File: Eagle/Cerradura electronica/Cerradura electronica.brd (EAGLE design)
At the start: 48.5 x 50 mm, 38 parts, among them IC1 LD117AS50TR, Q1 2N3904, Q2 IRF540NS, U1 ATMEGA328P_TQFP

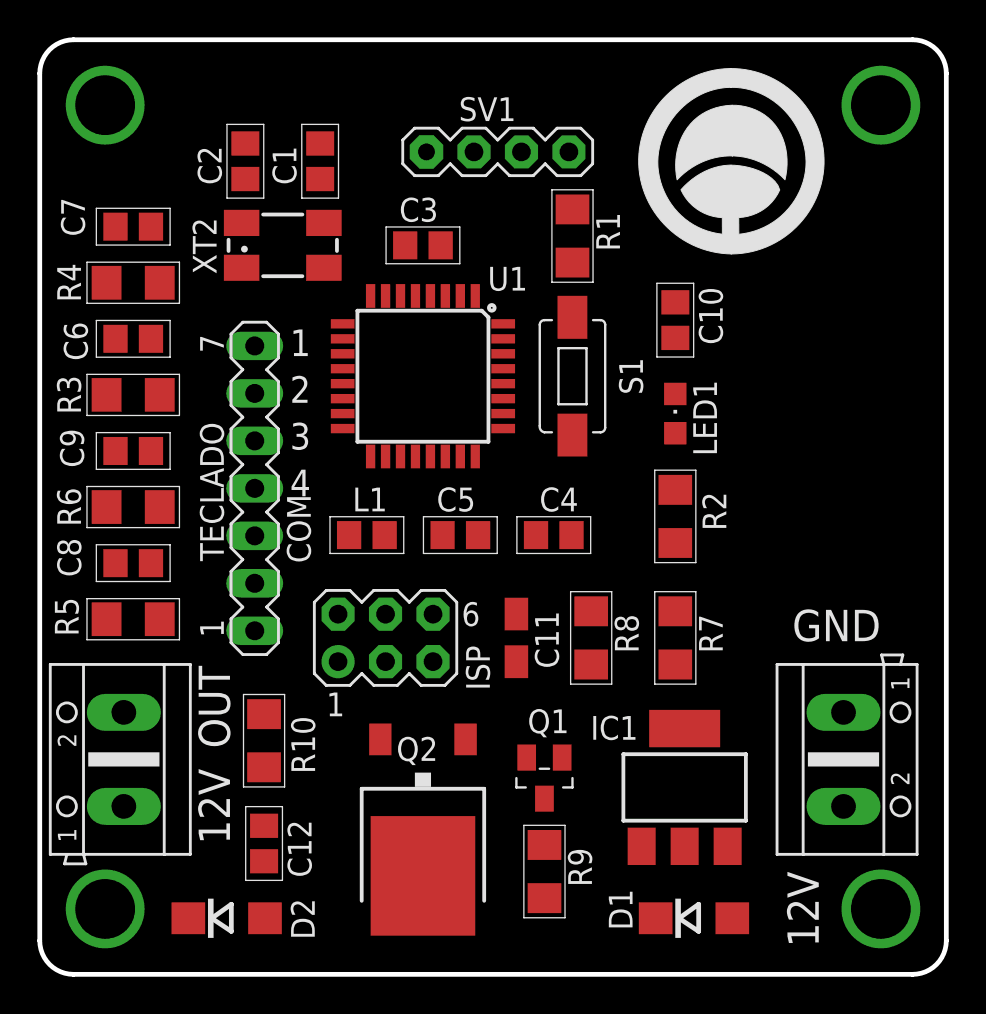
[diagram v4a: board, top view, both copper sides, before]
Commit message: Terminado ruteo, inicio revision 1.0
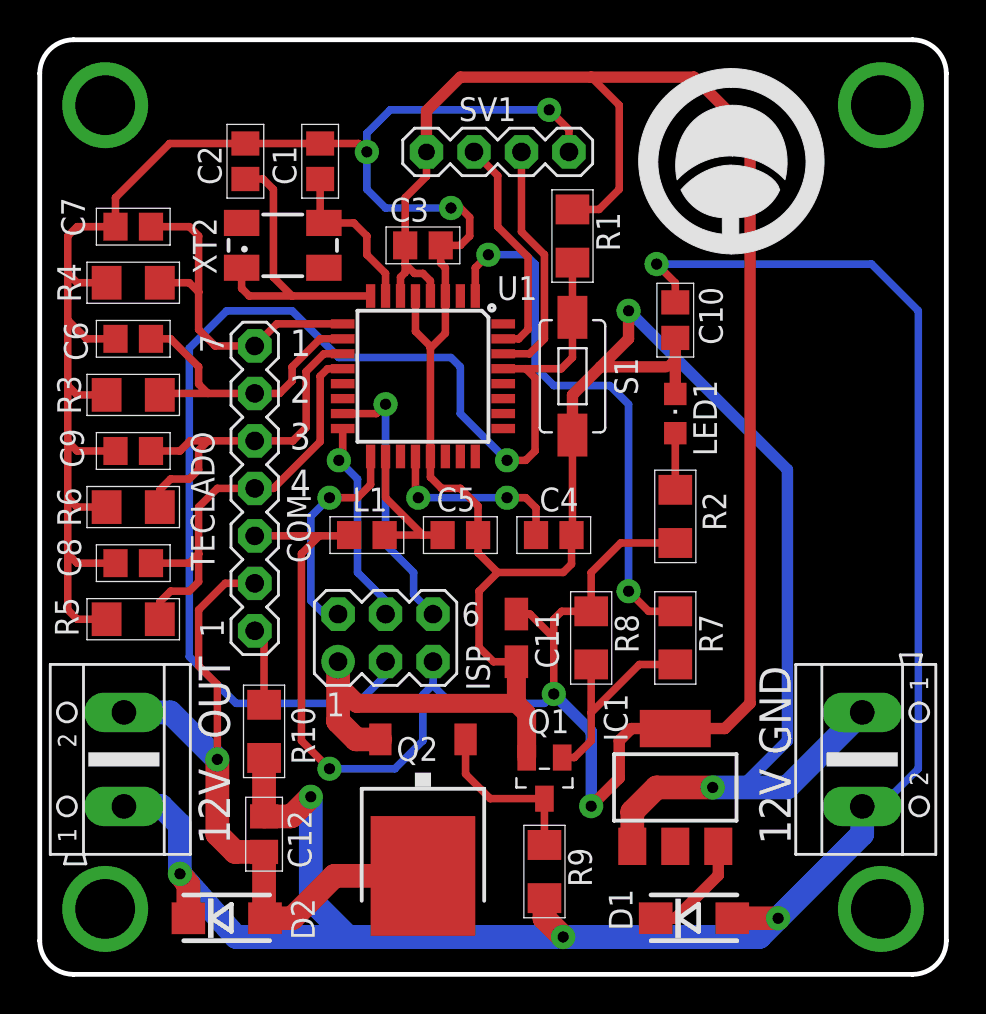
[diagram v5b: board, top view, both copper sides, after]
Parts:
- moved PWR 1.00 mm to (44.0, 11.5)
- moved C12 0.50 mm to (12.0, 7.50)
- moved IC1 0.50 mm to (34.0, 10.0)
- moved R10 0.50 mm to (12.0, 13.0)
- turned S1 to 90 degrees
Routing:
- net GND: track 0.00 -> 206.7 mm, vias 0 -> 5
- net VCC: track 0.00 -> 142.8 mm, vias 0 -> 3
- net +12V: track 0.00 -> 115.5 mm, vias 0 -> 5
- net RST: track 0.00 -> 67.3 mm, vias 0 -> 1
- net MOT_ON: track 0.00 -> 37.9 mm, vias 0 -> 1
- net D3: track 0.00 -> 29.5 mm, vias 0 -> 2
- net D8/3: track 0.00 -> 23.0 mm
- net D7/4: track 0.00 -> 19.4 mm
- net D5/2: track 0.00 -> 18.6 mm
- net D6/1: track 0.00 -> 16.3 mm
- net OS2: track 0.00 -> 16.0 mm
- net MOSI: track 0.00 -> 14.8 mm, vias 0 -> 1
- net RX1: track 0.00 -> 13.0 mm
- net TX0: track 0.00 -> 12.2 mm
- net SCK: track 0.00 -> 11.7 mm, vias 0 -> 1
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
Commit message: Terminado PCB teclado
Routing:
- net +12V: track 115.5 -> 116.4 mm
- added copper zone on layer 1, net GND
- added copper zone on layer 16, net GND
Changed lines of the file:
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@@
 </element>
 <element name="C5" library="rcl" package="C0805" value="1uF" x="22.5" y="23.5" smashed="yes">
-<attribute name="NAME" x="21.23" y="24.77" size="1.27" layer="25" ratio="10"/>
+<attribute name="NAME" x="21.73" y="24.77" size="1.27" layer="25" ratio="10"/>
 <attribute name="VALUE" x="21.23" y="20.96" size="1.27" layer="27"/>
 </element>
@@
 </element>
 <element name="Q2" library="Circuitos-Creativos-Transistores" package="TO-252" value="IRF540NS" x="20.5" y="6.5" smashed="yes" rot="R180">
-<attribute name="NAME" x="21.31" y="12.69" size="1.27" layer="25" ratio="10" rot="R180"/>
+<attribute name="NAME" x="21.81" y="12.69" size="1.27" layer="25" ratio="10" rot="R180"/>
 <attribute name="VALUE" x="15.42" y="10.31" size="1.27" layer="27" rot="R270"/>
 </element>
@@
 <wire x1="31.5" y1="34" x2="30" y2="32.5" width="0.6096" layer="1"/>
 <wire x1="33" y1="10" x2="36" y2="10" width="1.27" layer="1"/>
+<polygon width="0.6096" layer="1" isolate="1">
+<vertex x="-2" y="-2"/>
+<vertex x="50.5" y="-2"/>
+<vertex x="50.5" y="52"/>
+<vertex x="-2" y="52"/>
+</polygon>
+<polygon width="0.6096" layer="16" isolate="1">
+<vertex x="-1" y="-1"/>
+<vertex x="49.5" y="-1"/>
+<vertex x="49.5" y="51"/>
+<vertex x="-1" y="51"/>
+</polygon>
 </signal>
 <signal name="1">
@@
 <contactref element="R10" pad="1"/>
 <contactref element="PWR" pad="2"/>
-<wire x1="44" y1="8.9854" x2="44" y2="7.5" width="1.27" layer="16"/>
-<wire x1="44" y1="7.5" x2="39.5" y2="3" width="1.27" layer="16"/>
 <via x="39.5" y="3" extent="1-16" drill="0.6" shape="octagon"/>
 <wire x1="39.5" y1="3" x2="37.05" y2="3" width="1.27" layer="1"/>
@@
 <wire x1="47" y1="11" x2="44.9854" y2="8.9854" width="0.4064" layer="16"/>
 <wire x1="44.9854" y1="8.9854" x2="44" y2="8.9854" width="0.4064" layer="16"/>
+<wire x1="44" y1="8.9854" x2="42.4854" y2="8.9854" width="1.27" layer="16"/>
+<wire x1="42.4854" y1="8.9854" x2="41.5" y2="8" width="1.27" layer="16"/>
+<wire x1="41.5" y1="8" x2="41.5" y2="5" width="1.27" layer="16"/>
+<wire x1="41.5" y1="5" x2="39.5" y2="3" width="1.27" layer="16"/>
 </signal>
 <signal name="N$2">

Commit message: Cambio solicitado por Segcontrol SAS
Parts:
- C10: device rcl:C0805 -> rcl:C1206
- C11: device rcl:R/2012-12W -> rcl:C1206
- R10: value 10k -> 1k
- XT2: device crystal:CTS406 -> crystal:SM49
- moved C3 10.4 mm to (30.5, 42.0)
- moved C1 4.61 mm to (18.5, 46.5)
- moved C2 3.91 mm to (13.5, 46.5)
- moved XT2 3.61 mm to (16.0, 41.0)
- moved SV1 3.20 mm to (26.5, 46.5)
- moved R1 2.50 mm to (30.5, 38.0), turned to 0 degrees
- moved C10 1.12 mm to (34.5, 34.0)
- moved S1 1.00 mm to (28.5, 31.0)
- moved U$1 0.90 mm to (37.8, 44.0)
- moved LED1 0.71 mm to (34.5, 29.5)
- moved R2 0.50 mm to (34.5, 24.5)
- moved R7 0.50 mm to (34.5, 18.0)
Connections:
- net +12V: no longer R10.1
- net GND: now also C11.2, TECLADO.2; no longer C11.-
- net MOT_ON: no longer TECLADO.2
- net OS1: now also XT2.2; no longer XT2.3
- net VCC: now also C11.1, R10.1; no longer C11.+
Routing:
- net GND: track 206.7 -> 249.1 mm, vias 5 -> 3
- net VCC: track 142.8 -> 125.3 mm, vias 3 -> 5
- net MOT_ON: track 37.9 -> 25.9 mm
- net +12V: track 116.4 -> 111.3 mm
- net D3: track 29.5 -> 34.2 mm
- net OS1: track 8.64 -> 12.9 mm
- net RST: track 67.3 -> 70.4 mm
- net RX1: track 13.0 -> 15.4 mm
- net TX0: track 12.2 -> 14.1 mm
- net D5/2: track 18.6 -> 17.8 mm
- net N$2: track 11.6 -> 12.1 mm
- net N$1: track 3.03 -> 2.53 mm
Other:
- board text added: "CERRADURA"
- board text added: "ELECTRONICA"
- board text added: "v1.5.0"

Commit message: Etapa de potencia con activacion GPS y teclado simultanea
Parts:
- R7: value 1k -> 150R
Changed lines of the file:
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@@
 <attribute name="VALUE" x="38.285" y="16.58" size="1.778" layer="27" ratio="10" rot="R270"/>
 </element>
-<element name="R7" library="rcl" package="R1206" value="1k" x="34.5" y="18" smashed="yes" rot="R270">
+<element name="R7" library="rcl" package="R1206" value="150R" x="34.5" y="18" smashed="yes" rot="R270">
 <attribute name="NAME" x="35.77" y="19.27" size="1.27" layer="25" ratio="10" rot="R270"/>
 <attribute name="VALUE" x="31.96" y="19.27" size="1.27" layer="27" rot="R270"/>
